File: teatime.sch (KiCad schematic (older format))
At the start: 90 parts, among them J1 PROG, Q1 2N7000, SW1 SW_Push, U1 MCP1700-3302E, U2 74HC595, U3 74HC595, U4 74HC595, U5 74HC595, U6 ATtiny85-20PU

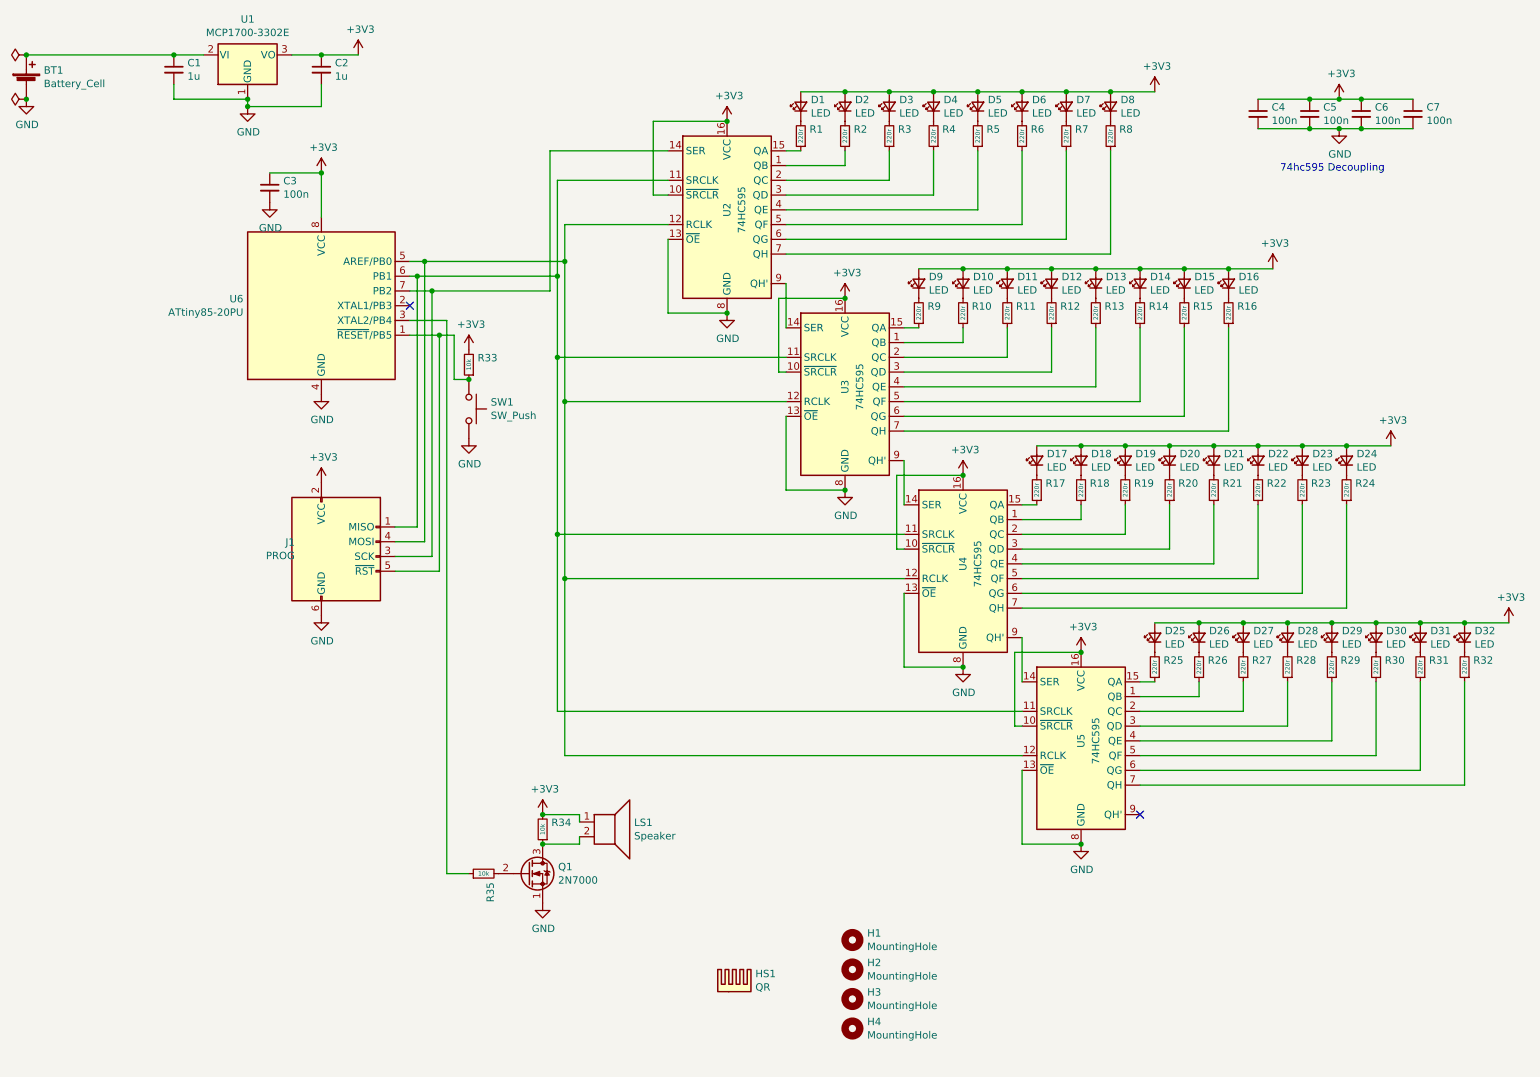
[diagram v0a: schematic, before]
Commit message: SMD variant board
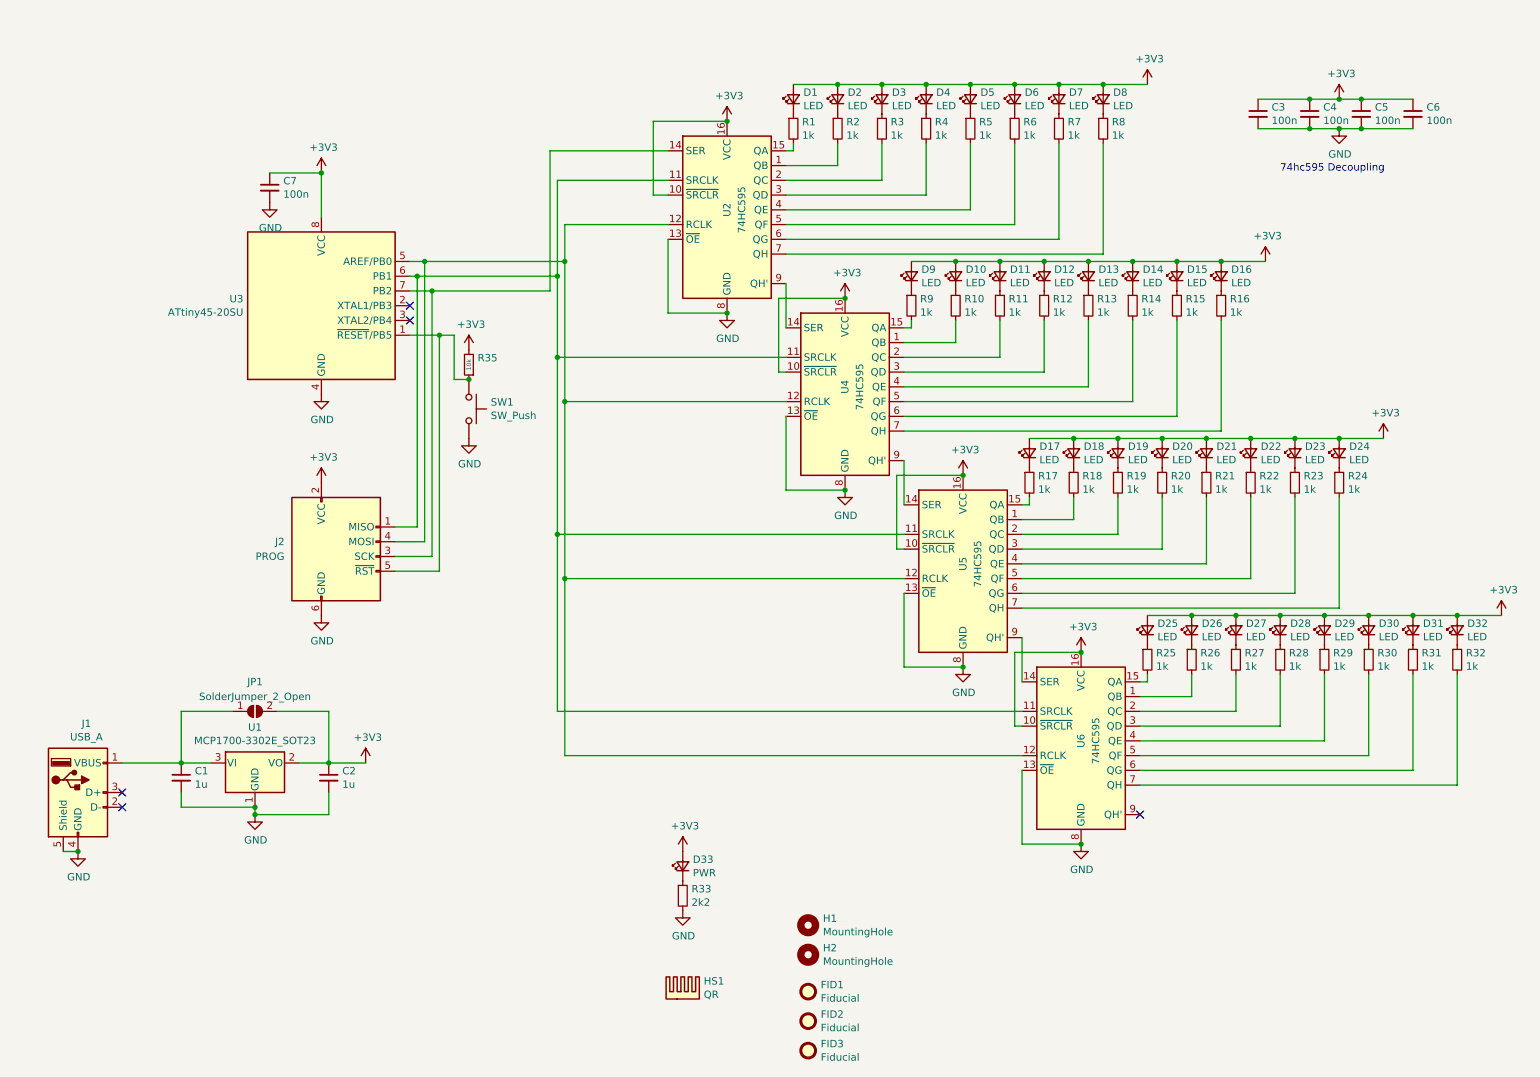
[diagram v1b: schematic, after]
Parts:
- removed BT1: Battery_Cell, Connector_JST:JST_PH_S2B-PH-K_1x02_P2.00mm_Horizontal, symbol Device:Battery_Cell
- removed H3, H4: MountingHole, MountingHole:MountingHole_3.2mm_M3, symbol Mechanical:MountingHole
- removed LS1: Speaker, Buzzer_Beeper:Buzzer_12x9.5RM7.6, symbol Device:Speaker
- removed Q1: 2N7000, Package_TO_SOT_THT:TO-92_Inline_W4.0mm_Horizontal_FlatSideDown, symbol Transistor_FET:2N7000
- removed R34, R35: 10k, Resistor_THT:R_Axial_DIN0204_L3.6mm_D1.6mm_P7.62mm_Horizontal, symbol Device:R_Small
- removed U1: MCP1700-3302E, Package_TO_SOT_THT:TO-92_Inline_W4.0mm_Horizontal_FlatSideDown, symbol Regulator_Linear:MCP1700-3302E_TO92
- removed U3: 74HC595, Package_DIP:DIP-16_W7.62mm, symbol 74xx:74HC595
- removed U6: ATtiny85-20PU, Package_DIP:DIP-8_W7.62mm, symbol teatime-rescue:ATtiny85-20PU-MCU_Microchip_ATtiny
- added D33: PWR, LED_SMD:LED_0805_2012Metric, symbol Device:LED_Small
- added FID1, FID2, FID3: Fiducial, Fiducial:Fiducial_0.75mm_Mask1.5mm, symbol Mechanical:Fiducial
- added J1: USB_A, teatime:USB_A_CNCTech_1001-011-01101_Horizontal_DoubleSided, symbol Connector:USB_A
- added JP1: SolderJumper_2_Open, Jumper:SolderJumper-2_P1.3mm_Open_RoundedPad1.0x1.5mm, symbol Jumper:SolderJumper_2_Open
- added R33: 2k2, Resistor_SMD:R_0603_1608Metric, symbol Device:R_Small
- added U1: MCP1700-3302E_SOT23, Package_TO_SOT_SMD:SOT-23, symbol Regulator_Linear:MCP1700-3302E_SOT23
- added U3: ATtiny45-20SU, Package_SO:SOIJ-8_5.3x5.3mm_P1.27mm, symbol MCU_Microchip_ATtiny:ATtiny45-20SU
- added U6: 74HC595, Package_SO:SOIC-16_3.9x9.9mm_P1.27mm, symbol 74xx:74HC595
- C1, C2: footprint Capacitor_THT:C_Rect_L4.6mm_W3.0mm_P2.50mm_MKS02_FKP02 -> Resistor_SMD:R_0603_1608Metric; Farnell 2544872 -> (none); LCSC (none) -> C105524
- C3: renamed from C4; footprint Capacitor_THT:C_Rect_L4.0mm_W2.5mm_P2.50mm -> Resistor_SMD:R_0603_1608Metric
- C4: renamed from C5; footprint Capacitor_THT:C_Rect_L4.0mm_W2.5mm_P2.50mm -> Resistor_SMD:R_0603_1608Metric
- C5: renamed from C6; footprint Capacitor_THT:C_Rect_L4.0mm_W2.5mm_P2.50mm -> Resistor_SMD:R_0603_1608Metric
- C6: renamed from C7; footprint Capacitor_THT:C_Rect_L4.0mm_W2.5mm_P2.50mm -> Resistor_SMD:R_0603_1608Metric
- C7: renamed from C3; footprint Capacitor_THT:C_Rect_L4.0mm_W2.5mm_P2.50mm -> Resistor_SMD:R_0603_1608Metric
- D1, D10, D11, D12, D13, D14, D15, D16, D17, D18, D19, D2, D20, D21, D22, D23, D24, D25, D26, D27, D28, D29, D3, D30, D31, D32, D4, D5, D6, D7, D8, D9: footprint LED_THT:LED_D5.0mm -> LED_SMD:LED_0805_2012Metric
- J2: renamed from J1; footprint Connector_PinHeader_2.54mm:PinHeader_2x03_P2.54mm_Vertical -> Connector_IDC:IDC-Header_2x03_P2.54mm_Vertical
- R1, R10, R11, R12, R13, R14, R15, R16, R17, R18, R19, R2, R20, R21, R22, R23, R24, R25, R26, R27, R28, R29, R3, R30, R31, R32, R4, R5, R6, R7, R8, R9: value 220r -> 1k; footprint Resistor_THT:R_Axial_DIN0204_L3.6mm_D1.6mm_P7.62mm_Horizontal -> Resistor_SMD:R_0603_1608Metric
- R35: renamed from R33; footprint Resistor_THT:R_Axial_DIN0204_L3.6mm_D1.6mm_P7.62mm_Horizontal -> Resistor_SMD:R_0603_1608Metric
- SW1: footprint teatime:B3F-40xx -> Button_Switch_THT:SW_PUSH_6mm
- U2, U4, U5: footprint Package_DIP:DIP-16_W7.62mm -> Package_SO:SOIC-16_3.9x9.9mm_P1.27mm; LCSC (none) -> C110383
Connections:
- net +3V3: now also D33.2 (A), JP1.2 (B), U1.2 (VO), U3.8 (VCC), U6.10 (~SRCLR), U6.16 (VCC)
- net GND: now also J1.4 (GND), J1.5 (Shield), R33.2, U1.1 (GND), U3.4 (GND), U6.13 (~OE), U6.8 (GND)
- net at U2.1 (QB): now also R2.2; no longer R2.1
- net at J2.1 (MISO), U2.11 (SRCLK), U4.11 (SRCLK)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: now also U3.6 (PB1), U6.11 (SRCLK)
- net at J2.4 (MOSI), U2.12 (RCLK), U4.12 (RCLK)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: now also U3.5 (AREF/PB0), U6.12 (RCLK)
- net at J2.3 (SCK), U2.14 (SER): now also U3.7 (PB2)
- net at U2.15 (QA): now also R1.2; no longer R1.1
- net at U2.2 (QC): now also R3.2; no longer R3.1
- net at U2.3 (QD): now also R4.2; no longer R4.1
- net at U2.4 (QE): now also R5.2; no longer R5.1
- net at U2.5 (QF): now also R6.2; no longer R6.1
- net at U2.6 (QG): now also R7.2; no longer R7.1
- net at U2.7 (QH): now also R8.2; no longer R8.1
- net at U2.9 (QH'): now also U4.14 (SER)
- net at D1.1 (K): now also R1.1; no longer R1.2
- net at D2.1 (K): now also R2.1; no longer R2.2
- net at D3.1 (K): now also R3.1; no longer R3.2
- net at D4.1 (K): now also R4.1; no longer R4.2
- net at D5.1 (K): now also R5.1; no longer R5.2
- net at D6.1 (K): now also R6.1; no longer R6.2
- net at D7.1 (K): now also R7.1; no longer R7.2
- net at D8.1 (K): now also R8.1; no longer R8.2
- net at R9.2: now also U4.15 (QA); no longer D9.1 (K)
- net at R10.2: now also U4.1 (QB); no longer D10.1 (K)
- net at R11.2: now also U4.2 (QC); no longer D11.1 (K)
- net at R12.2: now also U4.3 (QD); no longer D12.1 (K)
- net at R13.2: now also U4.4 (QE); no longer D13.1 (K)
- net at R14.2: now also U4.5 (QF); no longer D14.1 (K)
- net at R15.2: now also U4.6 (QG); no longer D15.1 (K)
- net at R16.2: now also U4.7 (QH); no longer D16.1 (K)
- net at R17.2: now also U5.15 (QA); no longer D17.1 (K)
- net at R18.2: now also U5.1 (QB); no longer D18.1 (K)
- net at R19.2: now also U5.2 (QC); no longer D19.1 (K)
- net at R20.2: now also U5.3 (QD); no longer D20.1 (K)
- net at R21.2: now also U5.4 (QE); no longer D21.1 (K)
- net at R22.2: now also U5.5 (QF); no longer D22.1 (K)
- net at R23.2: now also U5.6 (QG); no longer D23.1 (K)
- net at R24.2: now also U5.7 (QH); no longer D24.1 (K)
- net at R25.2: now also U6.15 (QA); no longer D25.1 (K)
- net at R26.2: now also U6.1 (QB); no longer D26.1 (K)
- net at R27.2: now also U6.2 (QC); no longer D27.1 (K)
- net at R28.2: now also U6.3 (QD); no longer D28.1 (K)
- net at R29.2: now also U6.4 (QE); no longer D29.1 (K)
- net at R30.2: now also U6.5 (QF); no longer D30.1 (K)
- net at R31.2: now also U6.6 (QG); no longer D31.1 (K)
- net at R32.2: now also U6.7 (QH); no longer D32.1 (K)
- net at R10.1: now also D10.1 (K)
- net at R9.1: now also D9.1 (K)
- net at R11.1: now also D11.1 (K)
- net at R12.1: now also D12.1 (K)
- net at R13.1: now also D13.1 (K)
- net at R14.1: now also D14.1 (K)
- net at R15.1: now also D15.1 (K)
- net at R16.1: now also D16.1 (K)
- net at R18.1: now also D18.1 (K); no longer U4.1 (QB)
- net at R17.1: now also D17.1 (K); no longer U4.15 (QA)
- net at R19.1: now also D19.1 (K); no longer U4.2 (QC)
- net at R20.1: now also D20.1 (K); no longer U4.3 (QD)
- net at R21.1: now also D21.1 (K); no longer U4.4 (QE)
- net at R22.1: now also D22.1 (K); no longer U4.5 (QF)
- net at R23.1: now also D23.1 (K); no longer U4.6 (QG)
- net at R24.1: now also D24.1 (K); no longer U4.7 (QH)
- net at R26.1: now also D26.1 (K); no longer U5.1 (QB)
- net at R25.1: now also D25.1 (K); no longer U5.15 (QA)
- net at R27.1: now also D27.1 (K); no longer U5.2 (QC)
- net at R28.1: now also D28.1 (K); no longer U5.3 (QD)
- net at R29.1: now also D29.1 (K); no longer U5.4 (QE)
- net at R30.1: now also D30.1 (K); no longer U5.5 (QF)
- net at R31.1: now also D31.1 (K); no longer U5.6 (QG)
- net at R32.1: now also D32.1 (K); no longer U5.7 (QH)
- net at U5.9 (QH'): now also U6.14 (SER)
- net at C1.1: now also J1.1 (VBUS), JP1.1 (A), U1.3 (VI)
- net at J2.5 (~RST), R35.1, SW1.1: now also U3.1 (~RESET~/PB5)
- new net: D33.1 (K), R33.1
- no-connect marks 2 -> 5
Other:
- moved on the sheet: C1, C2, D1, D2, D3, D4, D5, D6, D7, D8

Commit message: Completed board
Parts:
- added LS1: Speaker, Buzzer_Beeper:Buzzer_15x7.5RM7.6, symbol Device:Speaker
- added Q1: 2N7002, Package_TO_SOT_SMD:SOT-23, symbol Transistor_FET:2N7002
- added R34, R36: 10k, Resistor_SMD:R_0603_1608Metric, symbol Device:R_Small
- C3, C4, C5, C6, C7: Farnell 1141775 -> (none); LCSC (none) -> C80516
- D1, D10, D11, D12, D13, D14, D15, D16, D17, D18, D19, D2, D20, D21, D22, D23, D24, D25, D26, D27, D28, D29, D3, D30, D31, D32, D33, D4, D5, D6, D7, D8, D9: LCSC (none) -> C130114
- J2: footprint Connector_IDC:IDC-Header_2x03_P2.54mm_Vertical -> Connector_PinHeader_2.54mm:PinHeader_2x03_P2.54mm_Vertical
- R1, R10, R11, R12, R13, R14, R15, R16, R17, R18, R19, R2, R20, R21, R22, R23, R24, R25, R26, R27, R28, R29, R3, R30, R31, R32, R4, R5, R6, R7, R8, R9: LCSC (none) -> C115325
- R33: LCSC (none) -> C163872
- R35: LCSC (none) -> C98220
- SW1: LCSC (none) -> C93151
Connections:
- net +3V3: now also LS1.1, R34.1
- net GND: now also Q1.2 (S)
- net at U3.3 (XTAL2/PB4): now also R36.2
- new net: Q1.1 (G), R36.1
- new net: LS1.2, Q1.3 (D), R34.2
- no-connect marks 5 -> 4

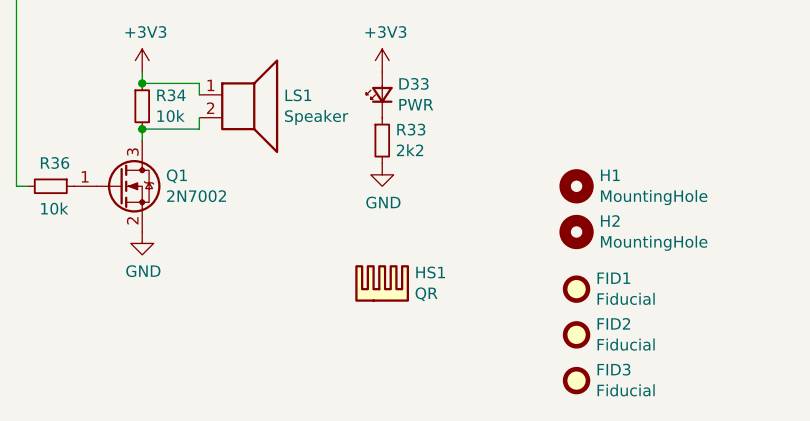
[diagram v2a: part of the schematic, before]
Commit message: Cant decoupling caps over
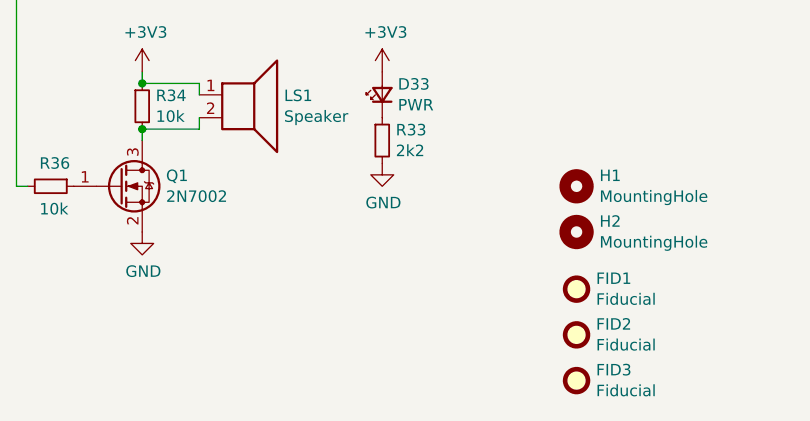
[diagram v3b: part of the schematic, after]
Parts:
- removed HS1: QR, teatime:__github.com_HarkonenBade_teatime, symbol Mechanical:Heatsink
- C1, C2, C3, C4, C5, C6, C7: footprint Resistor_SMD:R_0603_1608Metric -> Capacitor_SMD:C_0603_1608Metric
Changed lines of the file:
@@
 F 0 "C1" H 1842 5846 50  0000 L CNN
 F 1 "1u" H 1842 5755 50  0000 L CNN
-F 2 "Resistor_SMD:R_0603_1608Metric" H 1750 5800 50  0001 C CNN
+F 2 "Capacitor_SMD:C_0603_1608Metric" H 1750 5800 50  0001 C CNN
 F 3 "~" H 1750 5800 50  0001 C CNN
 F 4 "C105524" H 1750 5800 50  0001 C CNN "LCSC"
@@
 F 0 "C7" H 2442 1846 50  0000 L CNN
 F 1 "100n" H 2442 1755 50  0000 L CNN
-F 2 "Resistor_SMD:R_0603_1608Metric" H 2350 1800 50  0001 C CNN
+F 2 "Capacitor_SMD:C_0603_1608Metric" H 2350 1800 50  0001 C CNN
 F 3 "~" H 2350 1800 50  0001 C CNN
 F 4 "" H 2350 1800 50  0001 C CNN "Farnell"
@@
 F 0 "C3" H 9142 1346 50  0000 L CNN
 F 1 "100n" H 9142 1255 50  0000 L CNN
-F 2 "Resistor_SMD:R_0603_1608Metric" H 9050 1300 50  0001 C CNN
+F 2 "Capacitor_SMD:C_0603_1608Metric" H 9050 1300 50  0001 C CNN
 F 3 "~" H 9050 1300 50  0001 C CNN
 F 4 "" H 9050 1300 50  0001 C CNN "Farnell"
@@
 F 0 "C4" H 9492 1346 50  0000 L CNN
 F 1 "100n" H 9492 1255 50  0000 L CNN
-F 2 "Resistor_SMD:R_0603_1608Metric" H 9400 1300 50  0001 C CNN
+F 2 "Capacitor_SMD:C_0603_1608Metric" H 9400 1300 50  0001 C CNN
 F 3 "~" H 9400 1300 50  0001 C CNN
 F 4 "" H 9400 1300 50  0001 C CNN "Farnell"
@@
 F 0 "C5" H 9842 1346 50  0000 L CNN
 F 1 "100n" H 9842 1255 50  0000 L CNN
-F 2 "Resistor_SMD:R_0603_1608Metric" H 9750 1300 50  0001 C CNN
+F 2 "Capacitor_SMD:C_0603_1608Metric" H 9750 1300 50  0001 C CNN
 F 3 "~" H 9750 1300 50  0001 C CNN
 F 4 "" H 9750 1300 50  0001 C CNN "Farnell"
@@
 F 0 "C6" H 10192 1346 50  0000 L CNN
 F 1 "100n" H 10192 1255 50  0000 L CNN
-F 2 "Resistor_SMD:R_0603_1608Metric" H 10100 1300 50  0001 C CNN
+F 2 "Capacitor_SMD:C_0603_1608Metric" H 10100 1300 50  0001 C CNN
 F 3 "~" H 10100 1300 50  0001 C CNN
 F 4 "" H 10100 1300 50  0001 C CNN "Farnell"
@@
 F 0 "C2" H 2842 5846 50  0000 L CNN
 F 1 "1u" H 2842 5755 50  0000 L CNN
-F 2 "Resistor_SMD:R_0603_1608Metric" H 2750 5800 50  0001 C CNN
+F 2 "Capacitor_SMD:C_0603_1608Metric" H 2750 5800 50  0001 C CNN
 F 3 "~" H 2750 5800 50  0001 C CNN
 F 4 "C105524" H 2750 5800 50  0001 C CNN "LCSC"
@@
 	1    0    0    -1
 $EndComp
-$Comp
-L Mechanical:Heatsink HS1
-U 1 1 5F60161F
-P 5150 7300
-F 0 "HS1" H 5292 7421 50  0000 L CNN
-F 1 "QR" H 5292 7330 50  0000 L CNN
-F 2 "teatime:__github.com_HarkonenBade_teatime" H 5291 7284 50  0001 L CNN
-F 3 "~" H 5162 7300 50  0001 C CNN
-	1    5150 7300
-	1    0    0    -1
-$EndComp
